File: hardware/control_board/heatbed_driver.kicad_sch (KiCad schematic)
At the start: 10 parts, among them J3 Heatbed, Q1 IRLZ44N, U1 PC817

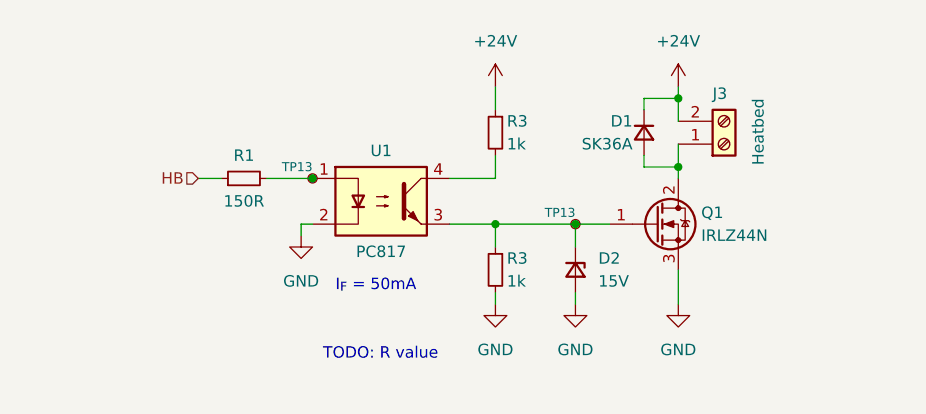
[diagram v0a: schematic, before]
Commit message: Adjust component values
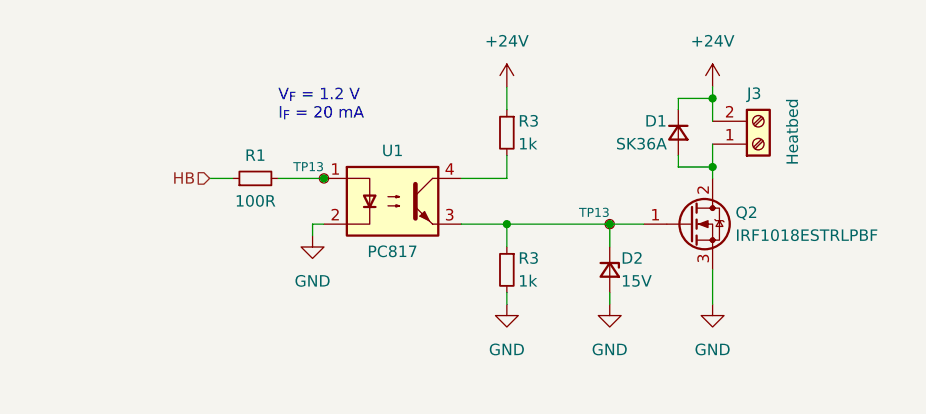
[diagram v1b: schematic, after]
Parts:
- removed Q1: IRLZ44N, Package_TO_SOT_THT:TO-220-3_Vertical, symbol Transistor_FET:IRLZ44N
- added Q2: IRF1018ESTRLPBF, Package_TO_SOT_SMD:TO-263-2, symbol Device:Q_NMOS_GDS
- D2: footprint (none) -> Diode_SMD:D_0603_1608Metric
- R1: value 150R -> 100R
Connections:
- net GND: now also Q2.3 (S)
- net at D2.1 (K), R3.1, TP13.1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: now also Q2.1 (G)
- net at D1.2 (A), J3.1 (Pin_1): now also Q2.2 (D)
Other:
- note added: "V_{F} = 1.2 V I_{F} = 20 mA"
- note removed: "I_{F} = 50mA"
- note removed: "TODO: R value"
- moved on the sheet: D1, D2, J3, R1, R3, TP13, U1

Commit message: Assign footprints to components
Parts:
- removed U1: PC817, Package_SO:SSO-4_6.7x5.1mm_P2.54mm_Clearance8mm, symbol Isolator:PC817
- added U8: TLP183, Package_SO:SOIC-4_4.55x3.7mm_P2.54mm, symbol Isolator:TLP185
- D2: footprint Diode_SMD:D_0603_1608Metric -> Diode_SMD:D_SOD-123F; Component (none) -> BZT52H-C15,115
- J3: footprint TerminalBlock:TerminalBlock_bornier-2_P5.08mm -> Local_Library:DG301-5.0-02P-11-00A; Component (none) -> DG301-5.0-02P-11-00A(H)
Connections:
- net GND: now also U8.3
- net at R1.2, TP13.1: now also U8.1
- net at D2.1 (K), Q2.1 (G), R3.1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: now also U8.4
- net at R3.2: now also U8.6
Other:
- note added: "V_{F} = 1.25 V I_{F} = 20 mA"
- note removed: "V_{F} = 1.2 V I_{F} = 20 mA"
- moved on the sheet: D1, D2, J3, Q2, R1, R3, TP13

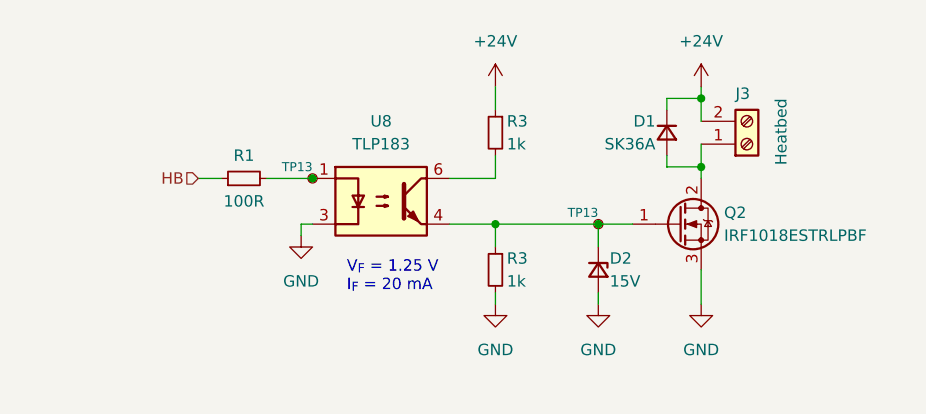
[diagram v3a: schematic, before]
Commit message: Place components on the control board PCB
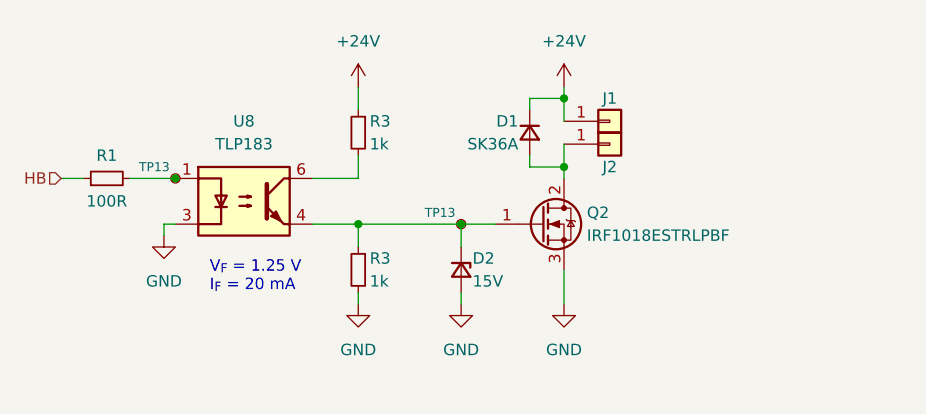
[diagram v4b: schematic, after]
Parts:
- removed J3: Heatbed, Local_Library:DG301-5.0-02P-11-00A, symbol Connector:Screw_Terminal_01x02
- added J1, J2: Conn_01x01, Local_Library:Pad_D5mm_H2.2mm, symbol Connector_Generic:Conn_01x01
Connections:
- net +24V: now also J1.1 (Pin_1)
- net at D1.2 (A), Q2.2 (D): now also J2.1 (Pin_1)
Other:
- moved on the sheet: D1, D2, Q2, R1, R3, TP13, U8

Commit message: Route front panel PCB tracks
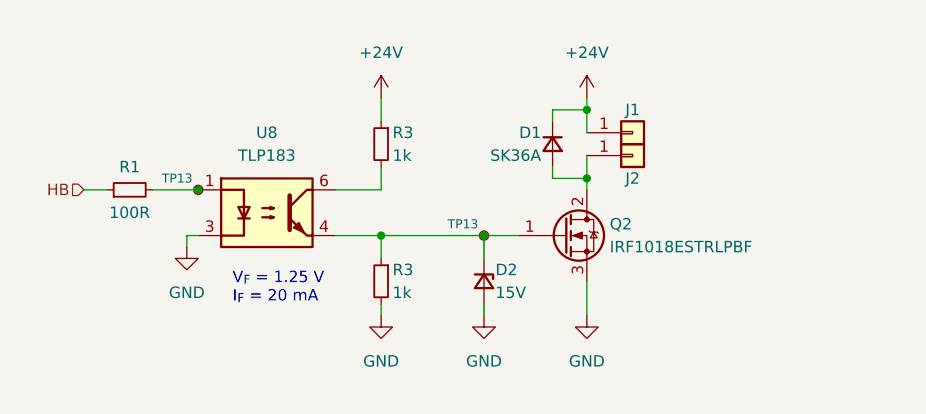
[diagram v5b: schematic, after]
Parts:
- TP13: now left out of the parts list
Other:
- moved on the sheet: D1, D2, J1, J2, Q2, R1, R3, TP13, U8

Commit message: Route control board PCB tracks
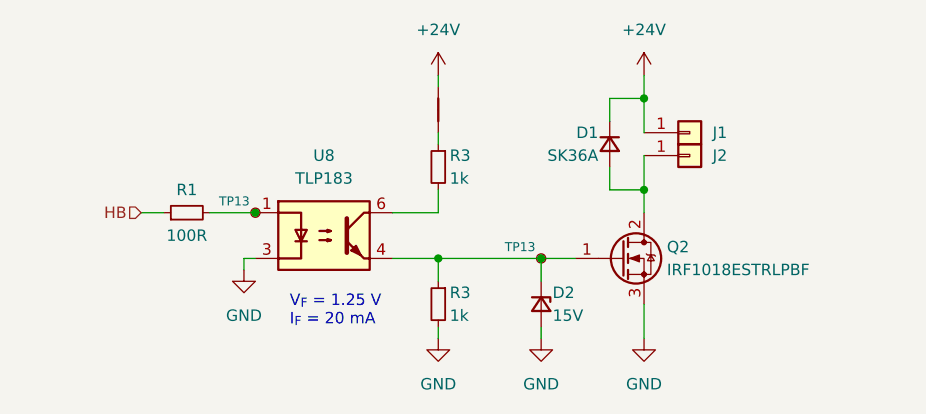
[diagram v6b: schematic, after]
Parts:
- added NT2: NetTie_2, Local_Library:NetTie-2_SMD_Pad0.2mm, symbol Device:NetTie_2
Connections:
- net +24V: now also NT2.2; no longer R3.1
- new net: NT2.1, R3.1
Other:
- moved on the sheet: D1, D2, J1, J2, Q2, R1, R3, TP13, U8

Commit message: Fix DRC errors
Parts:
- J1, J2: footprint Local_Library:Pad_D5mm_H2.2mm -> Local_Library:Pad_D5mm_H2.2mm_Via
- U8: footprint Package_SO:SOIC-4_4.55x3.7mm_P2.54mm -> Local_Library:SOIC-4_4.55x3.7mm_P2.54mm
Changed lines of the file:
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@@
       (effects (font (size 1.27 1.27)) hide)
     )
-    (property "Footprint" "Local_Library:Pad_D5mm_H2.2mm" (at 171.45 92.71 0)
+    (property "Footprint" "Local_Library:Pad_D5mm_H2.2mm_Via" (at 171.45 92.71 0)
       (effects (font (size 1.27 1.27)) hide)
     )
@@
       (effects (font (size 1.27 1.27)) hide)
     )
-    (property "Footprint" "Local_Library:Pad_D5mm_H2.2mm" (at 171.45 95.25 0)
+    (property "Footprint" "Local_Library:Pad_D5mm_H2.2mm_Via" (at 171.45 95.25 0)
       (effects (font (size 1.27 1.27)) hide)
     )
@@
       (effects (font (size 1.27 1.27)))
     )
-    (property "Footprint" "Package_SO:SOIC-4_4.55x3.7mm_P2.54mm" (at 130.81 111.76 0)
+    (property "Footprint" "Local_Library:SOIC-4_4.55x3.7mm_P2.54mm" (at 130.81 111.76 0)
       (effects (font (size 1.27 1.27) italic) hide)
     )

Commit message: Cleanup the project
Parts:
- D1: value SK36A -> SK310A
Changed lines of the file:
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@@
       (effects (font (size 1.27 1.27)) (justify left))
     )
-    (property "Value" "SK36A" (at 161.29 95.25 90)
+    (property "Value" "SK310A" (at 161.29 95.25 90)
       (effects (font (size 1.27 1.27)) (justify left))
     )
@@
       (effects (font (size 1.27 1.27)) hide)
     )
-    (property "Datasheet" "https://www.smc-diodes.com/propdf/SK36A%20N0104%20REV.A.pdf" (at 162.56 93.98 90)
+    (property "Datasheet" "https://www.smc-diodes.com/propdf/SK310A%20N0945%20REV.A.pdf" (at 162.56 93.98 90)
       (effects (font (size 1.27 1.27)) hide)
     )
